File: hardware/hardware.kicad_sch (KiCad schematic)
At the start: 0 parts

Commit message: Started working on relay driving circuit
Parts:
- added K1: RM85-2011-35-1005, Relpol:relpol_rm85_2011_35_1005, symbol Relpol:RM85-2011-35-1005
- added Q1: NPN, symbol Simulation_SPICE:NPN
- added R1: 100R, symbol Device:R
- added U1: XIAO-ESP32-C6, Seeed Studio:seeed_studio_xiao_esp32c6_dip, symbol Seeed Studio:XIAO_ESP32-C6-DIP
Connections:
- new net: Q1.2 (B), R1.2
- new net: K1.A1 (COIL_1), Q1.3 (E)
- new net +3V3: U1.12 (3V3)
- new net +5V: Q1.1 (C), U1.14 (VBUS)
- new net GND: K1.A2 (COIL_2), U1.13 (GND)
- new net RELAY_A_CTRL: R1.1, U1.1 (GPIO0/A0/D0)
- new net RELAY_B_CTRL: U1.2 (GPIO1/A1/D1)

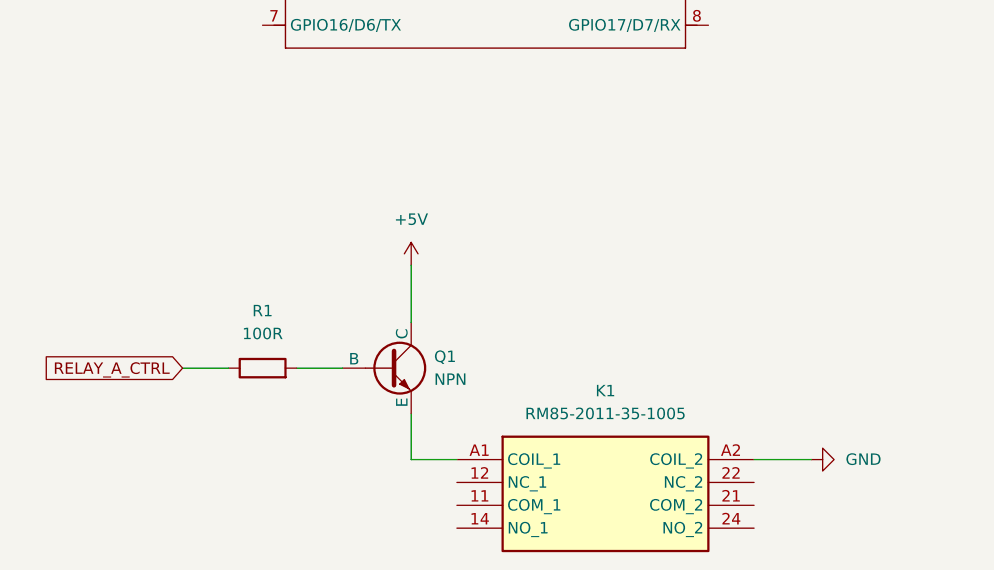
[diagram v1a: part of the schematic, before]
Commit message: Changed transitior orientation
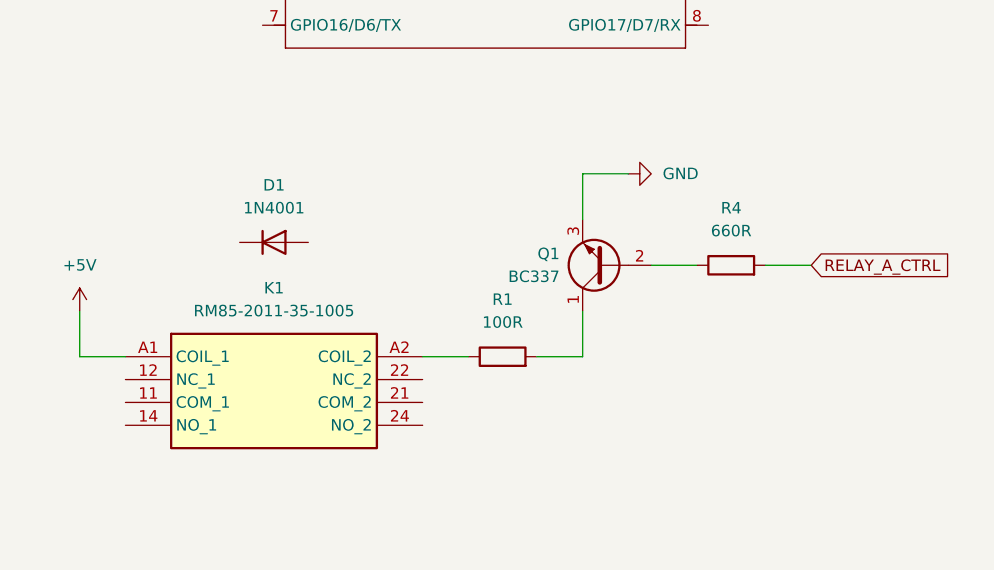
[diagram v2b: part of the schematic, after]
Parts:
- removed Q1: NPN, symbol Simulation_SPICE:NPN
- added D1: 1N4001, Diode_THT:D_DO-41_SOD81_P10.16mm_Horizontal, symbol Diode:1N4001
- added Q1: BC337, Package_TO_SOT_THT:TO-92_Inline, symbol Transistor_BJT:BC337
- added R4: 660R, symbol Device:R
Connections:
- net +5V: now also K1.A1 (COIL_1)
- net GND: now also Q1.3 (E); no longer K1.A2 (COIL_2)
- net RELAY_A_CTRL: now also R4.2; no longer R1.1
- net at R1.2: now also Q1.1 (C)
- new net: K1.A2 (COIL_2), R1.1
- new net: Q1.2 (B), R4.1
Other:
- moved on the sheet: K1

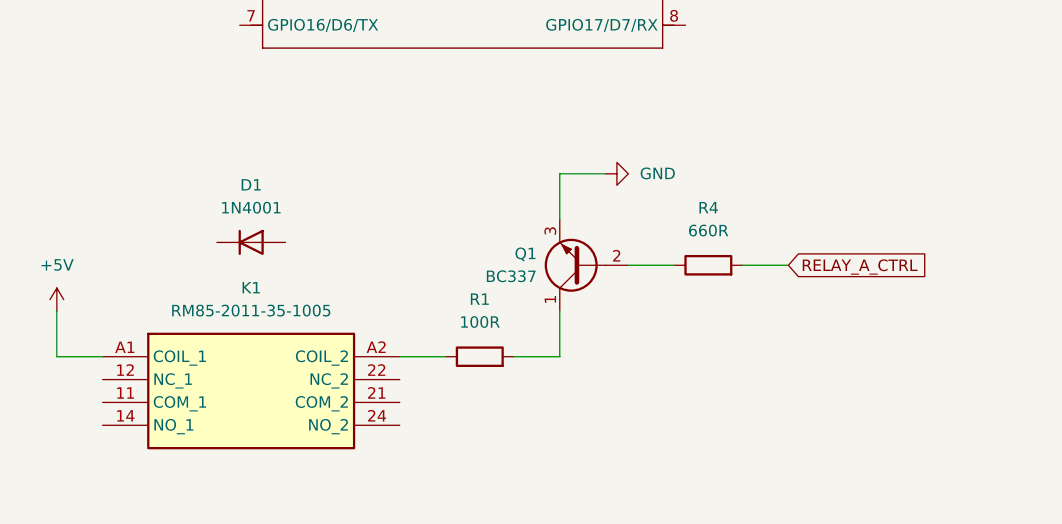
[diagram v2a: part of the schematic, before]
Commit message: Added relay flyback diode
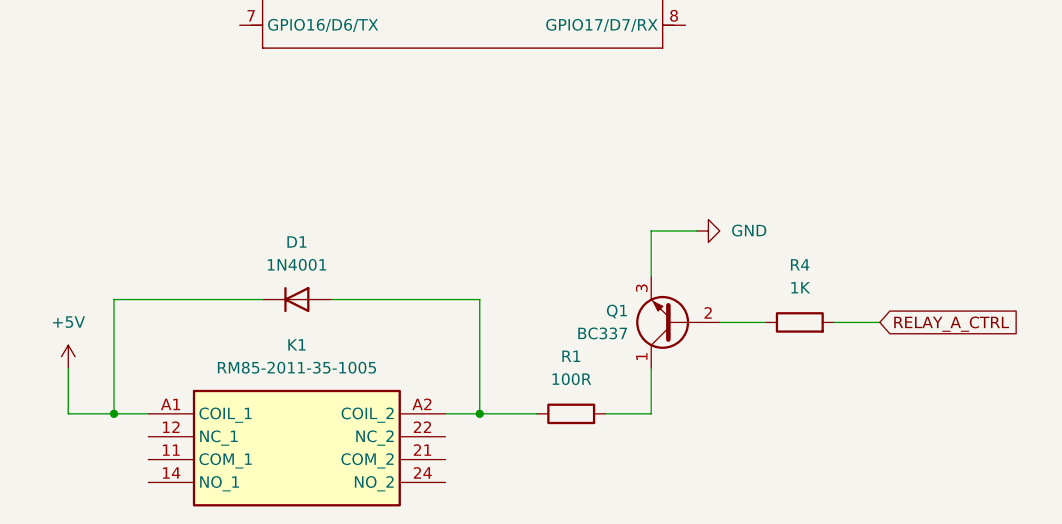
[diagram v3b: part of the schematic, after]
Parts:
- R4: value 660R -> 1K
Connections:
- net +5V: now also D1.1 (K)
- net at K1.A2 (COIL_2), R1.1: now also D1.2 (A)
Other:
- moved on the sheet: D1, K1, Q1, R1, R4

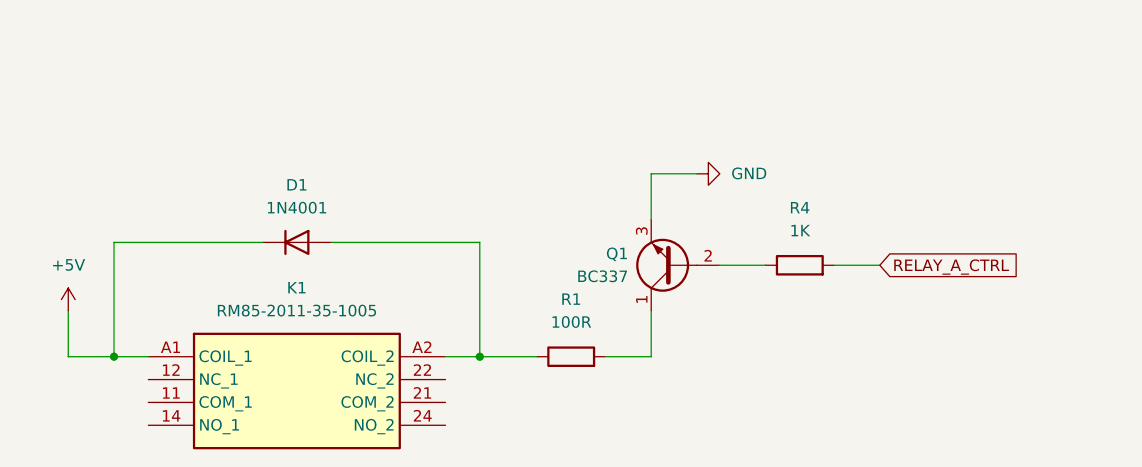
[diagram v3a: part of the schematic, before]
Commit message: Added pull-down resistor to relay control signal
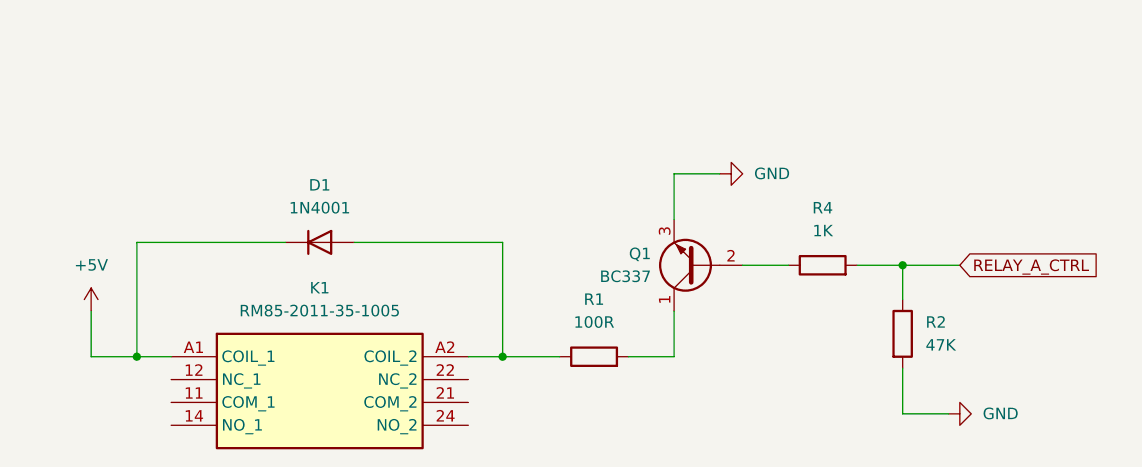
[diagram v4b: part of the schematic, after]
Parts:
- added R2: 47K, symbol Device:R
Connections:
- net GND: now also R2.2
- net RELAY_A_CTRL: now also R2.1
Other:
- moved on the sheet: D1, K1, Q1, R1, R4

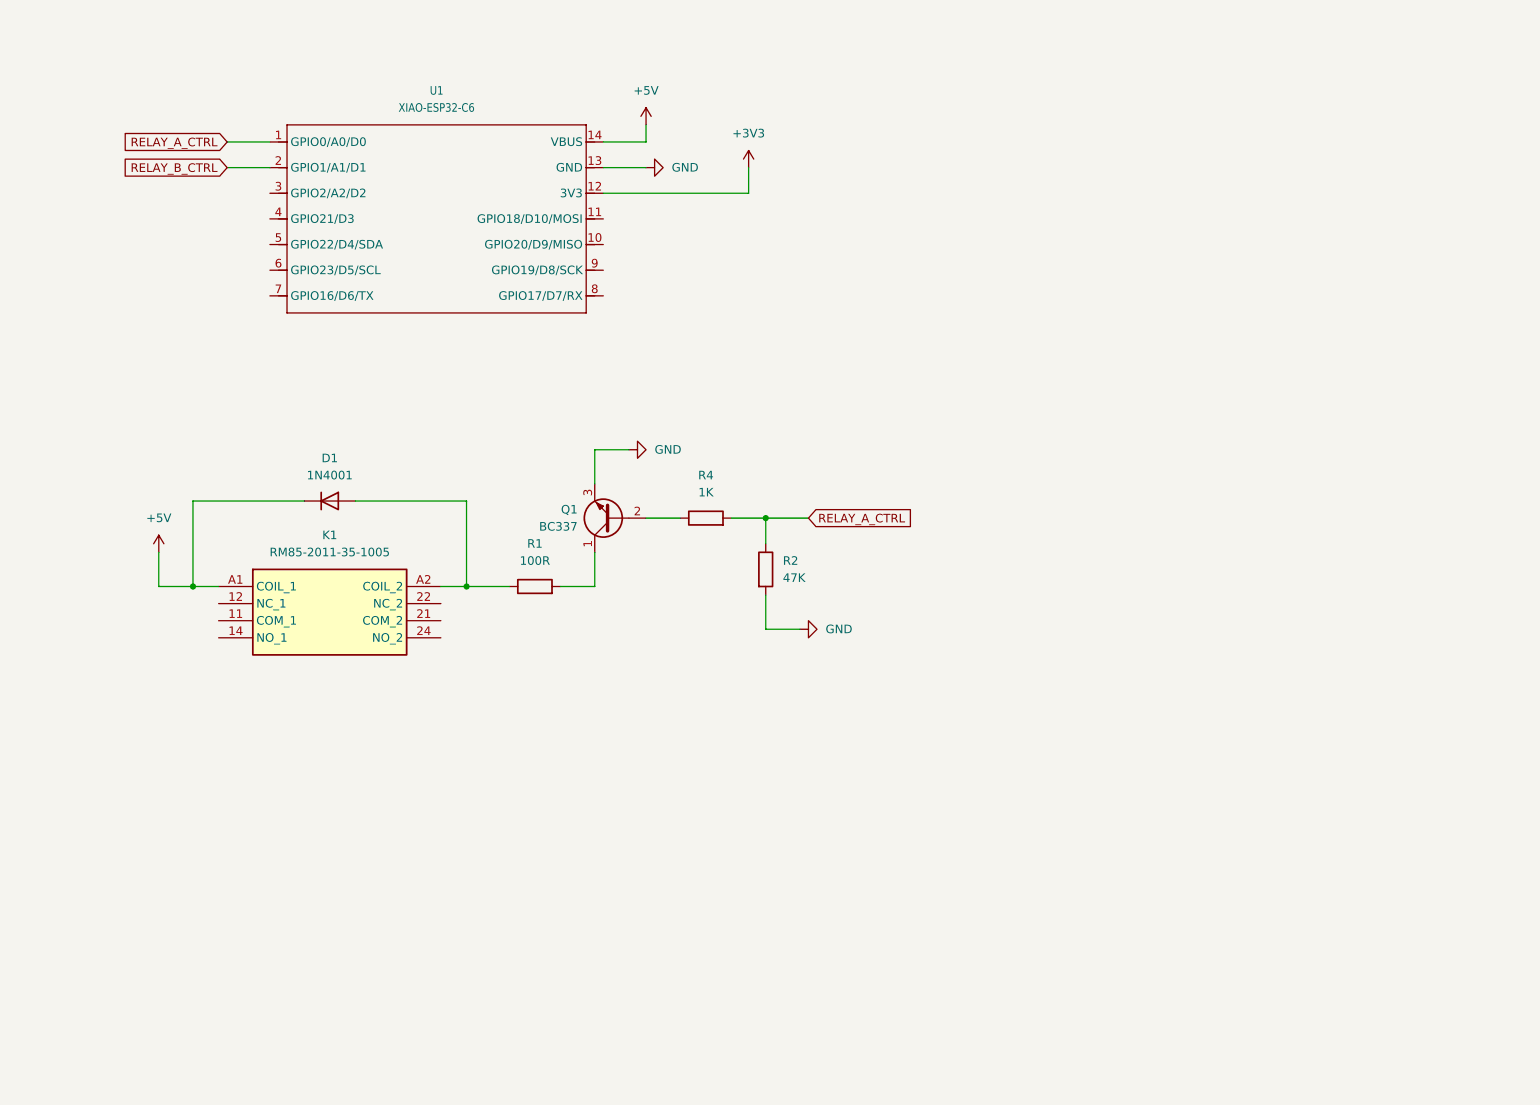
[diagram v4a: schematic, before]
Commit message: Added power supply
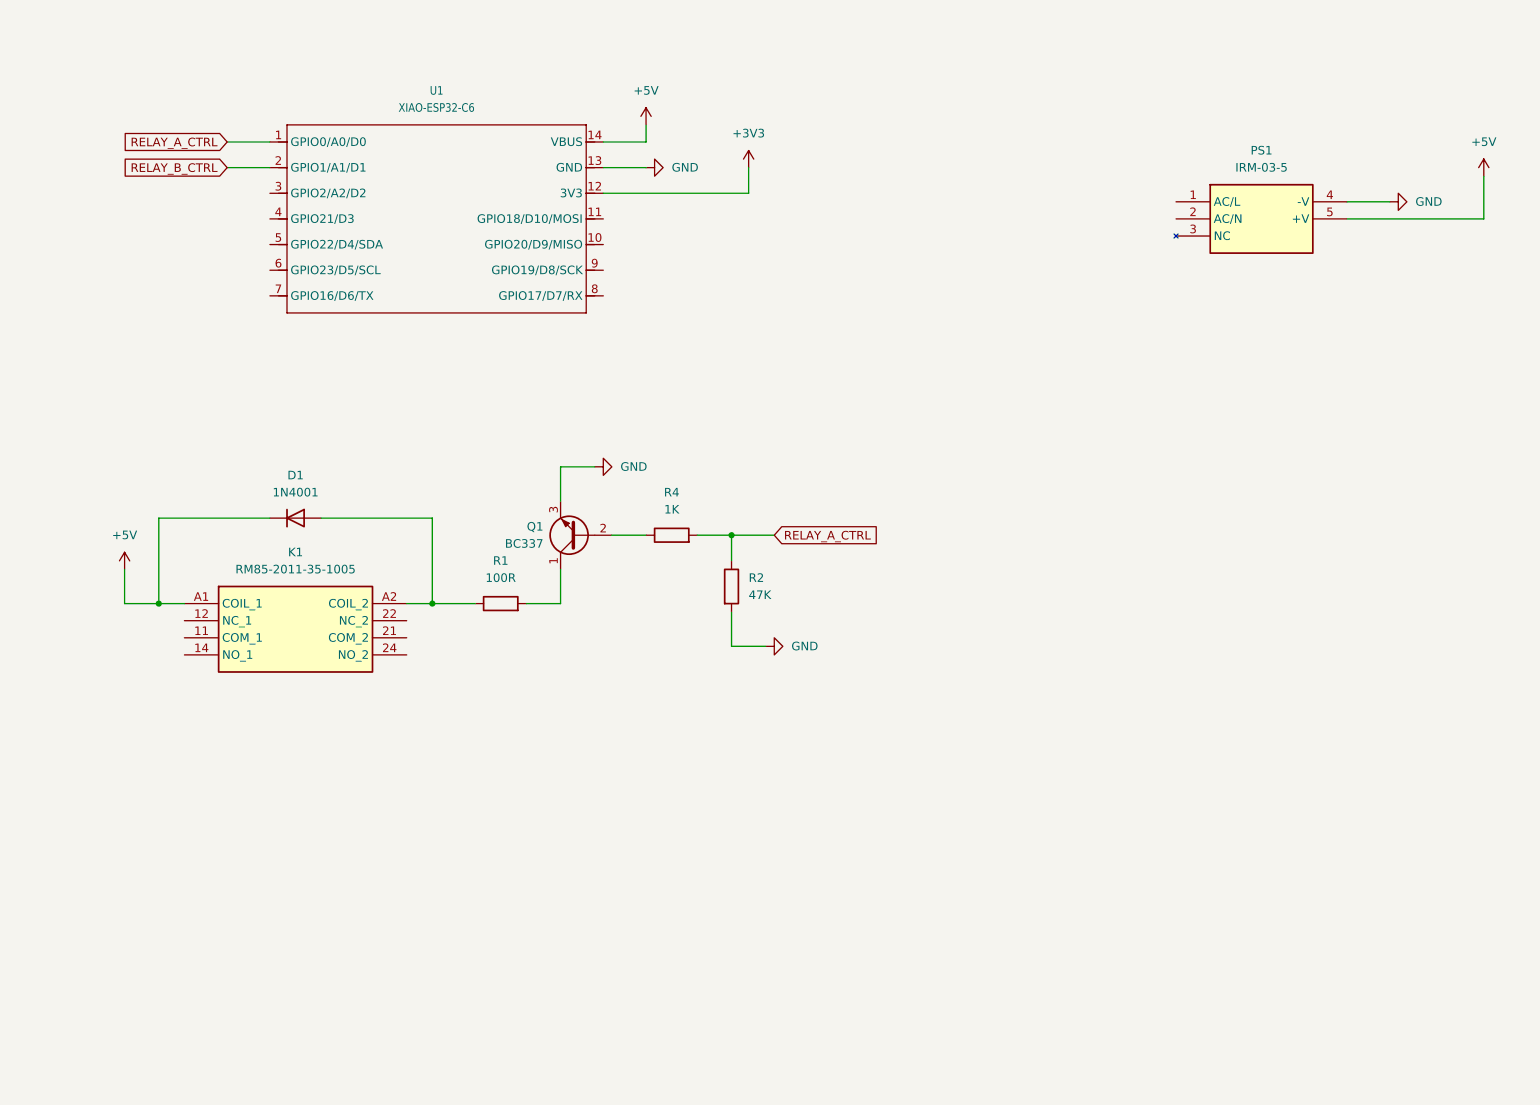
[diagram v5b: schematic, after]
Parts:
- added PS1: IRM-03-5, IRM0312, symbol Mean Well:IRM-03-5
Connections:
- net +5V: now also PS1.5 (+V)
- net GND: now also PS1.4 (-V)
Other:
- moved on the sheet: D1, K1, Q1, R1, R2, R4

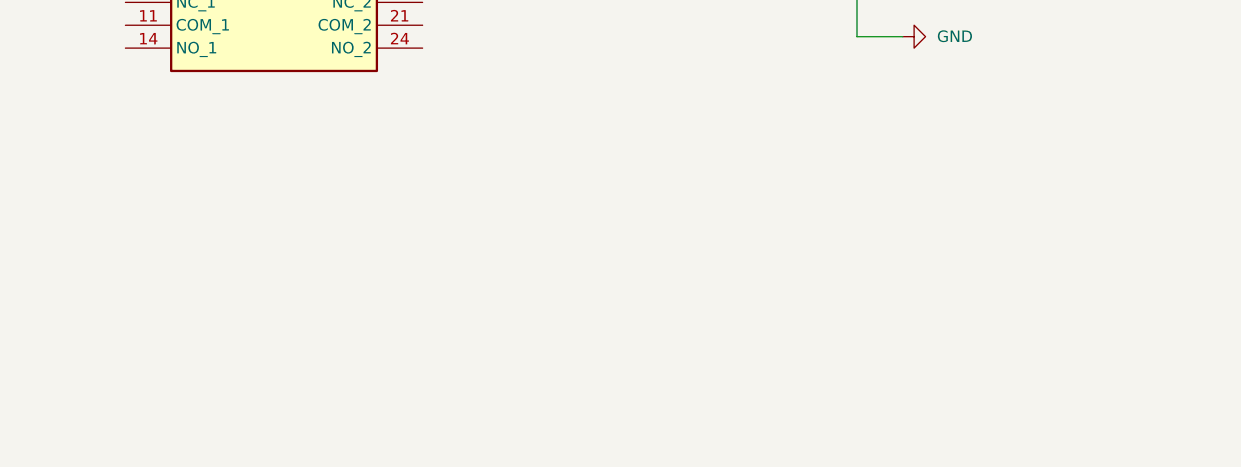
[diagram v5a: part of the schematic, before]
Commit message: Added second relay
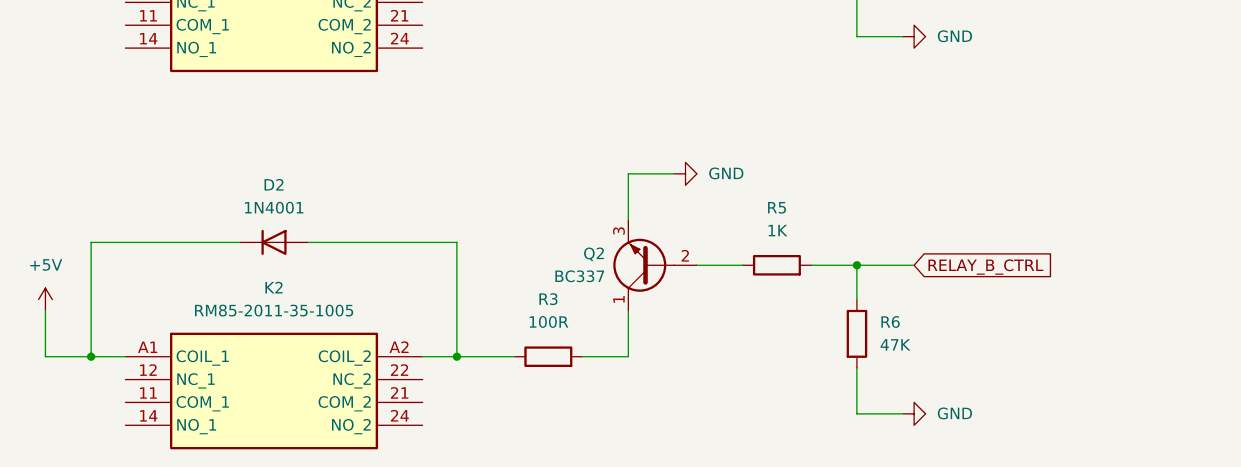
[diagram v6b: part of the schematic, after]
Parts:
- added D2: 1N4001, Diode_THT:D_DO-41_SOD81_P10.16mm_Horizontal, symbol Diode:1N4001
- added K2: RM85-2011-35-1005, Relpol:relpol_rm85_2011_35_1005, symbol Relpol:RM85-2011-35-1005
- added Q2: BC337, Package_TO_SOT_THT:TO-92_Inline, symbol Transistor_BJT:BC337
- added R3: 100R, symbol Device:R
- added R5: 1K, symbol Device:R
- added R6: 47K, symbol Device:R
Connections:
- net +5V: now also D2.1 (K), K2.A1 (COIL_1)
- net GND: now also Q2.3 (E), R6.2
- net RELAY_B_CTRL: now also R5.2, R6.1
- new net: D2.2 (A), K2.A2 (COIL_2), R3.1
- new net: Q2.2 (B), R5.1
- new net: Q2.1 (C), R3.2

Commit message: Added temperature sensor
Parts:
- added U2: DS18B20, Package_TO_SOT_THT:TO-92_Inline, symbol Sensor_Temperature:DS18B20
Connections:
- net +3V3: now also U2.3 (V_{DD})
- net GND: now also U2.1 (GND)
- net TEMP_SENSOR_DATA: now reaches U1.3 (GPIO2/A2/D2)
- net TEMP_SENSOR_DATA: now also U2.2 (DQ)
